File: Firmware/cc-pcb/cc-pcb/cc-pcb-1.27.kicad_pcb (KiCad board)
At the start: 2 copper layers, 31.5 x 33.5 mm, 25 parts, among them CON1 BARREL_JACK, IC1 ATMEGA328P-A, P1 CONN_20, P10 CONN_1, P11 CONN_1, P2 CONN_2, P4 CONN_1, P5 CONN_1, P6 CONN_1, P7 CONN_1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

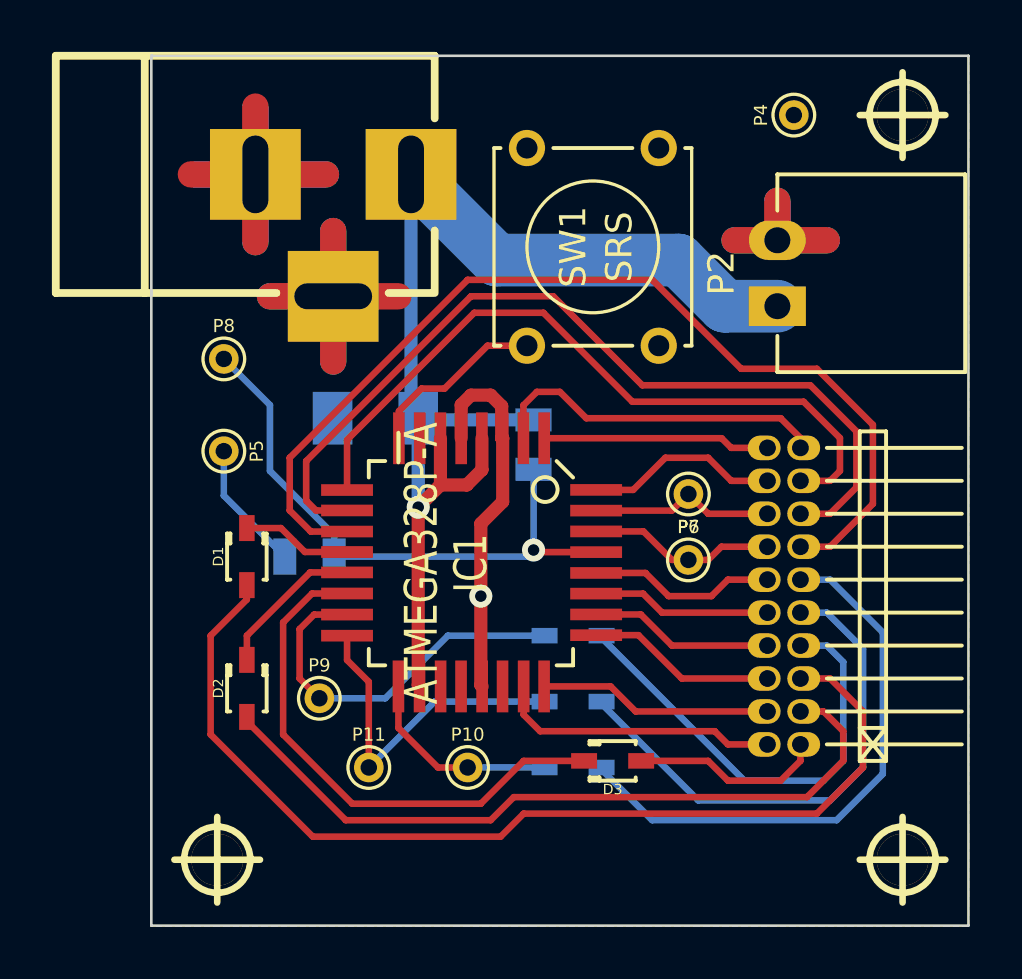
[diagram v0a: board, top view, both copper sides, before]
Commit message: added ref/values
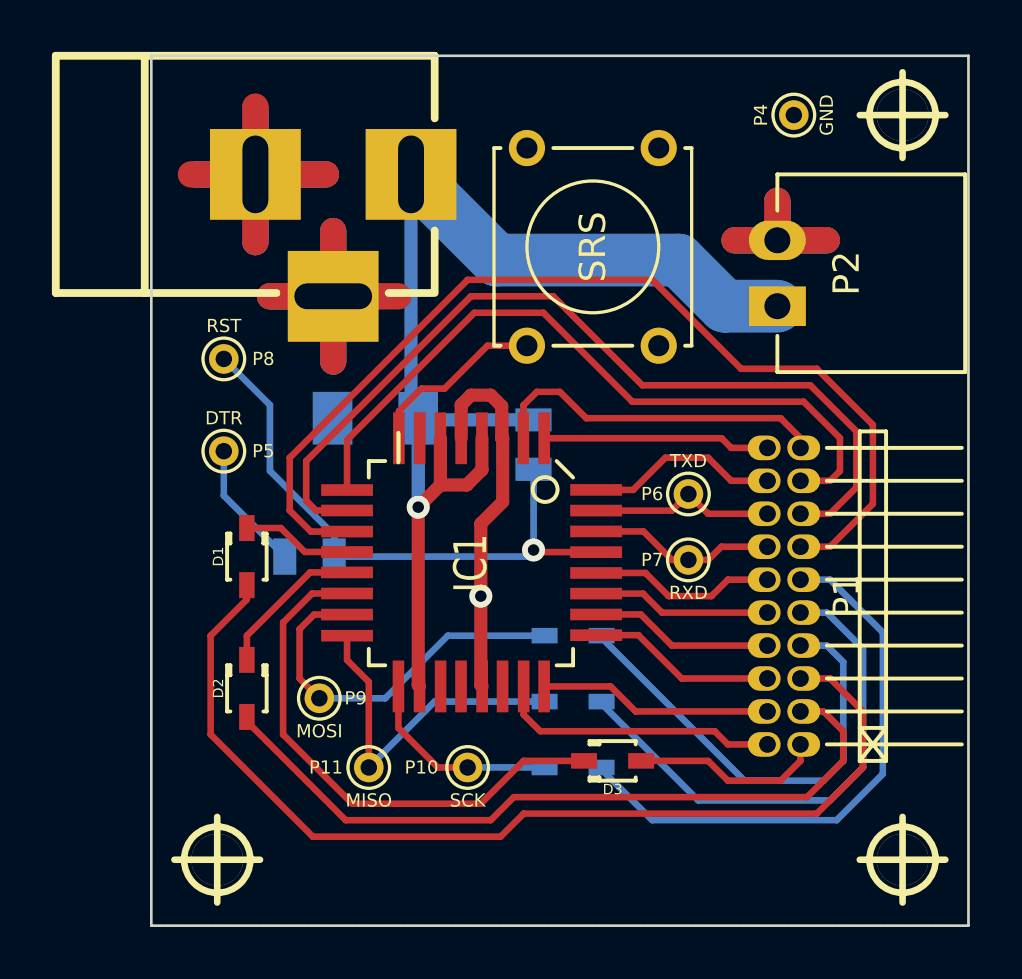
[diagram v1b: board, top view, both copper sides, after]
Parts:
- P10: value CONN_1 -> SCK
- P11: value CONN_1 -> MISO
- P4: value CONN_1 -> GND
- P5: value CONN_1 -> DTR
- P6: value CONN_1 -> TXD
- P7: value CONN_1 -> RXD
- P8: value CONN_1 -> RST
- P9: value CONN_1 -> MOSI
- turned P5 to 180 degrees
- turned P8 to 180 degrees
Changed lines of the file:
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@@
   (page A3)
   (layers
-    (15 F.Cu signal)
+    (15 F.Cu signal hide)
     (0 B.Cu signal hide)
     (16 B.Adhes user)
@@
     (pad_to_mask_clearance 0)
     (aux_axis_origin 100.076 100.076)
-    (visible_elements 7FFF9BFF)
+    (visible_elements 7FFFFBFF)
     (pcbplotparams
       (layerselection 284196865)
@@
     (at 108.712 114.046 180)
     (attr smd)
-    (fp_text reference C1 (at 0 0 180) (layer B.SilkS)
+    (fp_text reference C1 (at 0 1.905 180) (layer B.SilkS)
       (effects (font (size 0.762 0.762) (thickness 0.127)) (justify mirror))
     )
-    (fp_text value 10uF (at 0 0 180) (layer B.SilkS) hide
+    (fp_text value 10uF (at 0 -1.905 180) (layer B.SilkS)
       (effects (font (size 0.762 0.762) (thickness 0.127)) (justify mirror))
     )
@@
     (at 114.808 115.062 270)
     (attr smd)
-    (fp_text reference R1 (at 0 0.3175 270) (layer B.SilkS)
+    (fp_text reference R1 (at 0 1.524 270) (layer B.SilkS)
       (effects (font (size 0.50038 0.50038) (thickness 0.10922)) (justify mirror))
     )
-    (fp_text value 10k (at 0 -0.381 270) (layer B.SilkS)
+    (fp_text value 10k (at 0 -1.524 270) (layer B.SilkS)
       (effects (font (size 0.50038 0.50038) (thickness 0.10922)) (justify mirror))
     )
@@
     (at 106.172 119.38 180)
     (attr smd)
-    (fp_text reference C2 (at 0 0.3175 180) (layer B.SilkS)
+    (fp_text reference C2 (at 0 1.397 180) (layer B.SilkS)
       (effects (font (size 0.50038 0.50038) (thickness 0.10922)) (justify mirror))
     )
-    (fp_text value 0.1uF (at 0 -0.381 180) (layer B.SilkS)
+    (fp_text value 0.1uF (at 0 -1.524 180) (layer B.SilkS)
       (effects (font (size 0.50038 0.50038) (thickness 0.10922)) (justify mirror))
     )
@@
       (effects (font (size 1.27 1.016) (thickness 0.2032)))
     )
-    (fp_text value ATMEGA328P-A (at 0 1.905 270) (layer F.SilkS)
+    (fp_text value ATMEGA328P-A (at 0 1.905 270) (layer F.SilkS) hide
       (effects (font (size 1.27 1.016) (thickness 0.2032)))
     )
@@
   (module SW_PUSH_SMALL (layer F.Cu)
     (at 117.094 107.442 90)
-    (fp_text reference SW1 (at 0 -0.762 90) (layer F.SilkS)
+    (fp_text reference SW1 (at 0 -0.762 90) (layer F.SilkS) hide
       (effects (font (size 1.016 1.016) (thickness 0.2032)))
     )
-    (fp_text value SRS (at 0 1.016 90) (layer F.SilkS)
+    (fp_text value SRS (at 0 0 90) (layer F.SilkS)
       (effects (font (size 1.016 1.016) (thickness 0.2032)))
     )
@@
     (descr "Pin strip 1.27mm 10x2pin 90°")
     (tags "CONN DEV")
-    (fp_text reference P1 (at 0 -2.3 90) (layer F.SilkS) hide
+    (fp_text reference P1 (at 0 2.413 90) (layer F.SilkS)
       (effects (font (size 1 1) (thickness 0.15)))
     )
-    (fp_text value CONN_20 (at 0 -3.8 90) (layer F.SilkS) hide
+    (fp_text value CONN_20 (at 0 -2.286 90) (layer F.SilkS) hide
       (effects (font (size 1 1) (thickness 0.15)))
     )
@@
     (descr "module 1 pin (ou trou mecanique de percage)")
     (tags DEV)
-    (fp_text reference P7 (at 0 -1.26746) (layer F.SilkS)
-      (effects (font (size 0.508 0.508) (thickness 0.127)))
-    )
-    (fp_text value CONN_1 (at 0 1.27) (layer F.SilkS) hide
+    (fp_text reference P7 (at -1.397 0) (layer F.SilkS)
+      (effects (font (size 0.508 0.508) (thickness 0.127)))
+    )
+    (fp_text value RXD (at 0 1.27) (layer F.SilkS)
       (effects (font (size 0.508 0.508) (thickness 0.127)))
     )
@@
     (descr "module 1 pin (ou trou mecanique de percage)")
     (tags DEV)
-    (fp_text reference P6 (at 0 -1.26746 180) (layer F.SilkS)
-      (effects (font (size 0.508 0.508) (thickness 0.127)))
-    )
-    (fp_text value CONN_1 (at 0 1.27 180) (layer F.SilkS) hide
+    (fp_text reference P6 (at 1.397 0 180) (layer F.SilkS)
+      (effects (font (size 0.508 0.508) (thickness 0.127)))
+    )
+    (fp_text value TXD (at 0 1.27 180) (layer F.SilkS)
       (effects (font (size 0.508 0.508) (thickness 0.127)))
     )
@@
   )
   (module PINTST (layer F.Cu)
-    (at 102.87 115.316 270)
+    (at 102.87 115.316 180)
     (descr "module 1 pin (ou trou mecanique de percage)")
     (tags DEV)
-    (fp_text reference P5 (at 0 -1.26746 270) (layer F.SilkS)
-      (effects (font (size 0.508 0.508) (thickness 0.127)))
-    )
-    (fp_text value CONN_1 (at 0 1.27 270) (layer F.SilkS) hide
+    (fp_text reference P5 (at -1.524 0 180) (layer F.SilkS)
+      (effects (font (size 0.508 0.508) (thickness 0.127)))
+    )
+    (fp_text value DTR (at 0 1.27 180) (layer F.SilkS)
       (effects (font (size 0.508 0.508) (thickness 0.127)))
     )
     (fp_circle (center 0 0) (end -0.254 -0.762) (layer F.SilkS) (width 0.127))
-    (pad 1 thru_hole circle (at 0 0 270) (size 1.143 1.143) (drill 0.635)
+    (pad 1 thru_hole circle (at 0 0 180) (size 1.143 1.143) (drill 0.635)
       (layers *.Cu *.Mask F.SilkS)
       (net 4 N-0000012)
@@
       (effects (font (size 0.508 0.508) (thickness 0.127)))
     )
-    (fp_text value CONN_1 (at 0 1.27 90) (layer F.SilkS) hide
+    (fp_text value GND (at 0 1.27 90) (layer F.SilkS)
       (effects (font (size 0.508 0.508) (thickness 0.127)))
     )
@@
   (module XH2.54_2-90 (layer F.Cu)
     (at 124.206 108.458 90)
-    (fp_text reference P2 (at 0 -2.159 90) (layer F.SilkS)
+    (fp_text reference P2 (at 0 2.667 90) (layer F.SilkS)
       (effects (font (size 1.016 1.016) (thickness 0.2032)))
     )
@@
   )
   (module PINTST (layer F.Cu)
-    (at 102.87 111.76)
+    (at 102.87 111.76 180)
     (descr "module 1 pin (ou trou mecanique de percage)")
     (tags DEV)
-    (fp_text reference P8 (at 0 -1.26746) (layer F.SilkS)
-      (effects (font (size 0.508 0.508) (thickness 0.127)))
-    )
-    (fp_text value CONN_1 (at 0 1.27) (layer F.SilkS) hide
+    (fp_text reference P8 (at -1.524 0 180) (layer F.SilkS)
+      (effects (font (size 0.508 0.508) (thickness 0.127)))
+    )
+    (fp_text value RST (at 0 1.27 180) (layer F.SilkS)
       (effects (font (size 0.508 0.508) (thickness 0.127)))
     )
     (fp_circle (center 0 0) (end -0.254 -0.762) (layer F.SilkS) (width 0.127))
-    (pad 1 thru_hole circle (at 0 0) (size 1.143 1.143) (drill 0.635)
+    (pad 1 thru_hole circle (at 0 0 180) (size 1.143 1.143) (drill 0.635)
       (layers *.Cu *.Mask F.SilkS)
       (net 3 N-0000011)
@@
     (descr "module 1 pin (ou trou mecanique de percage)")
     (tags DEV)
-    (fp_text reference P9 (at 0 -1.26746) (layer F.SilkS)
-      (effects (font (size 0.508 0.508) (thickness 0.127)))
-    )
-    (fp_text value CONN_1 (at 0 1.27) (layer F.SilkS) hide
+    (fp_text reference P9 (at 1.397 0) (layer F.SilkS)
+      (effects (font (size 0.508 0.508) (thickness 0.127)))
+    )
+    (fp_text value MOSI (at 0 1.27) (layer F.SilkS)
       (effects (font (size 0.508 0.508) (thickness 0.127)))
     )
@@
     (descr "module 1 pin (ou trou mecanique de percage)")
     (tags DEV)
-    (fp_text reference P10 (at 0 -1.26746) (layer F.SilkS)
-      (effects (font (size 0.508 0.508) (thickness 0.127)))
-    )
-    (fp_text value CONN_1 (at 0 1.27) (layer F.SilkS) hide
+    (fp_text reference P10 (at -1.778 0) (layer F.SilkS)
+      (effects (font (size 0.508 0.508) (thickness 0.127)))
+    )
+    (fp_text value SCK (at 0 1.27) (layer F.SilkS)
       (effects (font (size 0.508 0.508) (thickness 0.127)))
     )
@@
     (descr "module 1 pin (ou trou mecanique de percage)")
     (tags DEV)
-    (fp_text reference P11 (at 0 -1.26746) (layer F.SilkS)
-      (effects (font (size 0.508 0.508) (thickness 0.127)))
-    )
-    (fp_text value CONN_1 (at 0 1.27) (layer F.SilkS) hide
-      (effects (font (size 0.508 0.508) (thickness 0.127)))
-    )
+    (fp_text reference P11 (at -1.651 0) (layer F.SilkS)
+      (effects (font (size 0.508 0.508) (thickness 0.127)))
+    )
+    (fp_text value MISO (at 0 1.27) (layer F.SilkS)
+      (effects (font (size 0.508 0.508) (thickness 0.127)))
+    )

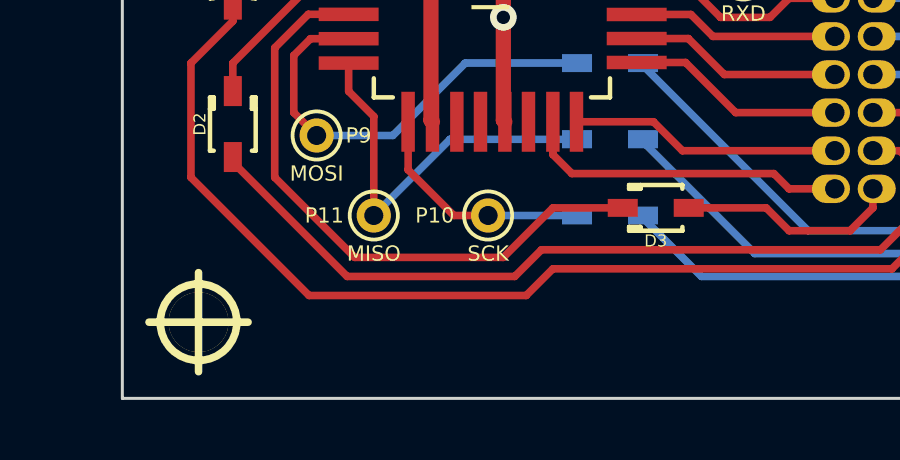
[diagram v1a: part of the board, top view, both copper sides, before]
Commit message: added 4DMC text
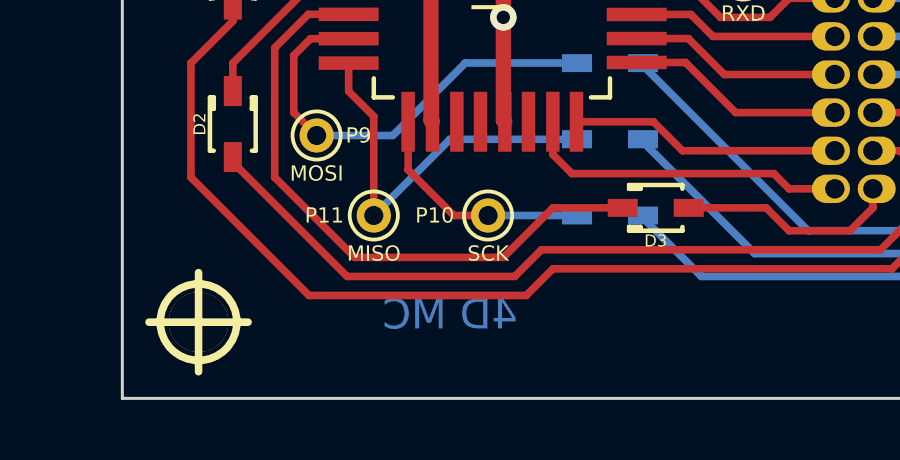
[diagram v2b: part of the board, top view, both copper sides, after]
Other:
- board text added: "4D MC"
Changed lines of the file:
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@@
-(kicad_pcb (version 3) (host pcbnew "(2014-01-10 BZR 4027)-stable")
+(kicad_pcb (version 3) (host pcbnew "(2013-07-07 BZR 4022)-stable")
   (general
     (links 52)
@@
     (area 95.734999 97.53092 132.028001 135.0264)
     (thickness 1.6)
-    (drawings 4)
+    (drawings 5)
     (tracks 221)
     (zones 0)
@@
   (layers
     (15 F.Cu signal hide)
-    (0 B.Cu signal hide)
+    (0 B.Cu signal)
     (16 B.Adhes user)
     (17 F.Adhes user)
@@
     (last_trace_width 0.254)
     (trace_clearance 0.254)
-    (zone_clearance 1.016)
+    (zone_clearance 0.508)
     (zone_45_only no)
     (trace_min 0.254)
@@
     )
   )
+  (gr_text "4D MC" (at 110.998 130.81) (layer B.Cu)
+    (effects (font (size 1 1) (thickness 0.2)) (justify mirror))
+  )
   (gr_line (start 100.076 133.604) (end 100.076 100.076) (angle 90) (layer Edge.Cuts) (width 0.1))

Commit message: finalizing pcb...
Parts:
- moved P4 0.68 mm to (124.2, 102.6)
- moved H1 0.25 mm to (129.0, 102.6)

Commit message: after dfm check
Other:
- net class Default: via_dia 0.889 -> 1.143
- net class PWR: via_dia 0.889 -> 3.302; via_drill 0.635 -> 1.27
- net class PWRIC: via_dia 0.889 -> 1.397; via_drill 0.635 -> 0.889
- net class PWRTHR: via_dia 0.889 -> 2.032; via_drill 0.635 -> 1.016

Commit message: after pcb to OSHPark submission
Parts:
- CON1: footprint BARREL_JACK -> BARREL_JACK_ROUND_PADS
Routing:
- net GND: track 62.7 -> 24.5 mm
